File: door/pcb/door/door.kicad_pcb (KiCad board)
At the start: 2 copper layers, 57.8 x 45.7 mm, 43 parts, among them J2 Conn_01x06_Male, J3 DB9_Female_MountingHoles, J4 Conn_01x03_Male, J5 Screw_Terminal_01x02, J6 Screw_Terminal_01x02, J7 Power_in, U1 10uF, U2 STM32F303CBTx, U3 SN65HVD230, Y1 8 Mhz

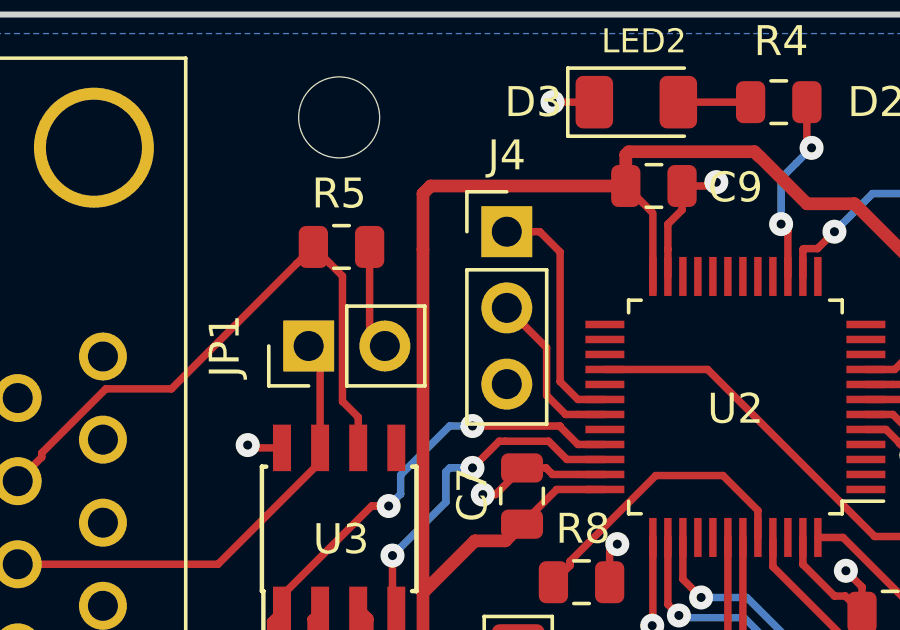
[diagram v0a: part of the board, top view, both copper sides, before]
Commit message: added silkscreen labels for the usart pin header
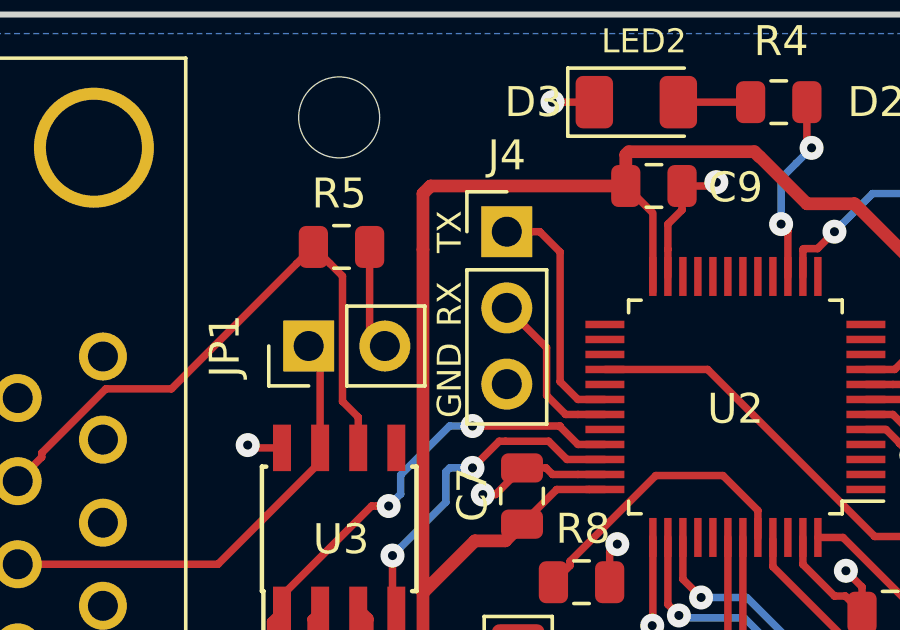
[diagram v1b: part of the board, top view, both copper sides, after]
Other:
- board text added: "RX"
- board text added: "TX"
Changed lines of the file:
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@@
   (general
     (thickness 1.6)
-    (drawings 25)
+    (drawings 28)
     (tracks 394)
     (zones 0)
@@
       (net 48 CAN_RX))
   )
+  (gr_text TX (at 113.919 78.994 90) (layer F.SilkS)
+    (effects (font (size 0.8 0.8) (thickness 0.1)))
+  )
+  (gr_text RX (at 113.919 81.407 90) (layer F.SilkS)
+    (effects (font (size 0.8 0.8) (thickness 0.1)))
+  )
+  (gr_text GND (at 113.919 83.947 90) (layer F.SilkS)
+    (effects (font (size 0.8 0.8) (thickness 0.1)))
+  )
   (gr_text "door V0.2" (at 124.46 93.472) (layer B.SilkS)

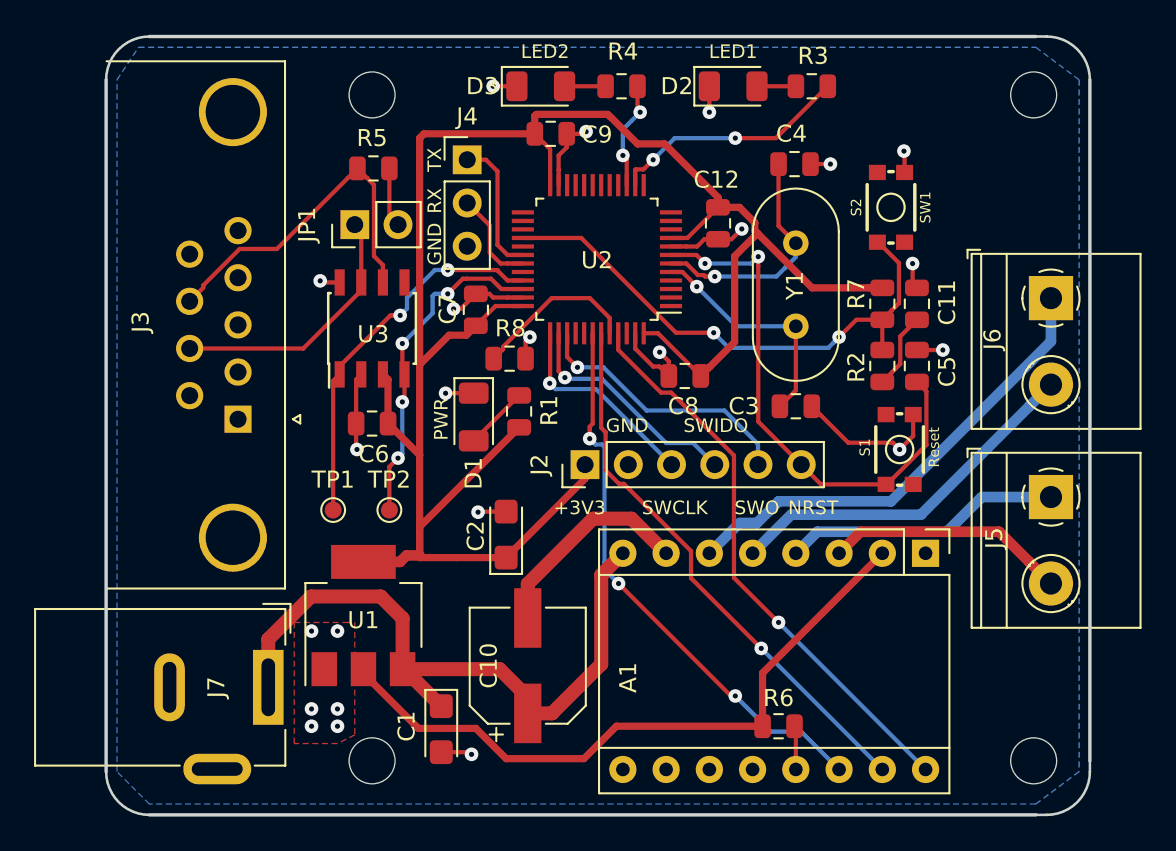
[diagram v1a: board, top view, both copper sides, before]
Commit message: changed pinout of DB-9 connector
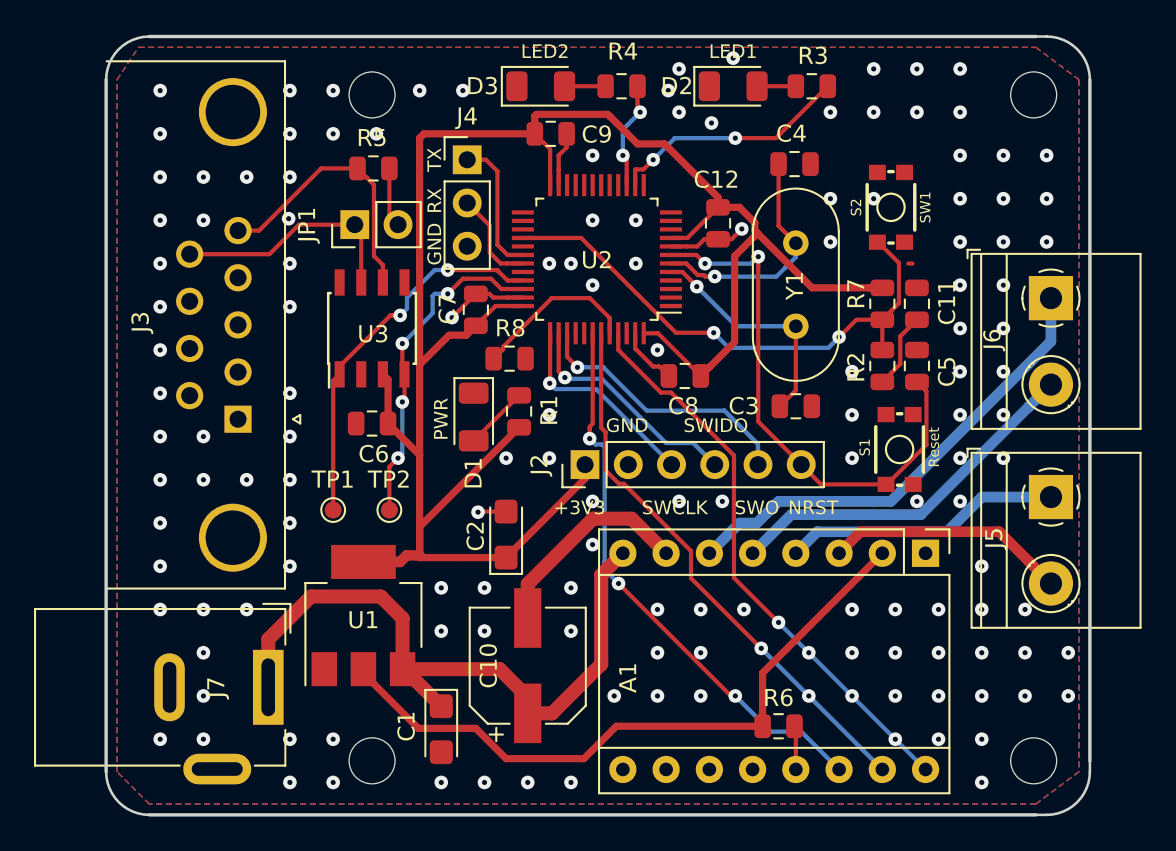
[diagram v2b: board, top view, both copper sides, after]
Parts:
- R1: value 250 -> 360
- U1: value 10uF -> LM1117DTX
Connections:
- J3 pad 1: Net-(J3-Pad1) -> GND
- J3 pad 5: GND -> /mcu/CANL
- J3 pad 7: /mcu/CANH -> Net-(J3-Pad7)
- J3 pad 8: /mcu/CANL -> Net-(J3-Pad8)
- J3 pad 9: Net-(J3-Pad9) -> /mcu/CANH
- J7 pad 1: +9V -> Net-(D4-Pad2)
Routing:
- net GND: track 60.8 -> 31.0 mm, vias 23 -> 140
- net /mcu/CANL: track 20.5 -> 15.8 mm
- net /mcu/CANH: track 15.5 -> 14.4 mm
- net DIR: vias 1 -> 4
- net STEP: vias 1 -> 2
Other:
- board text added: "door V0.3"
- board text removed: "door V0.2"

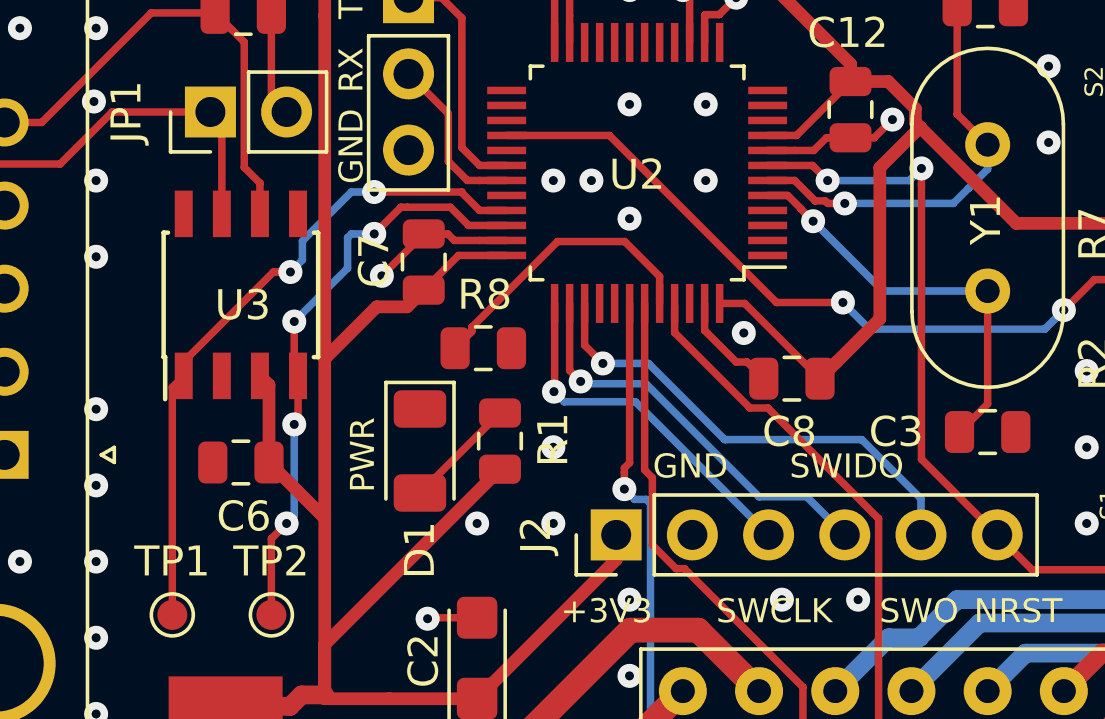
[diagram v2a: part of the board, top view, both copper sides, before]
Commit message: corrected error in Layout swido was connected with Can Rx
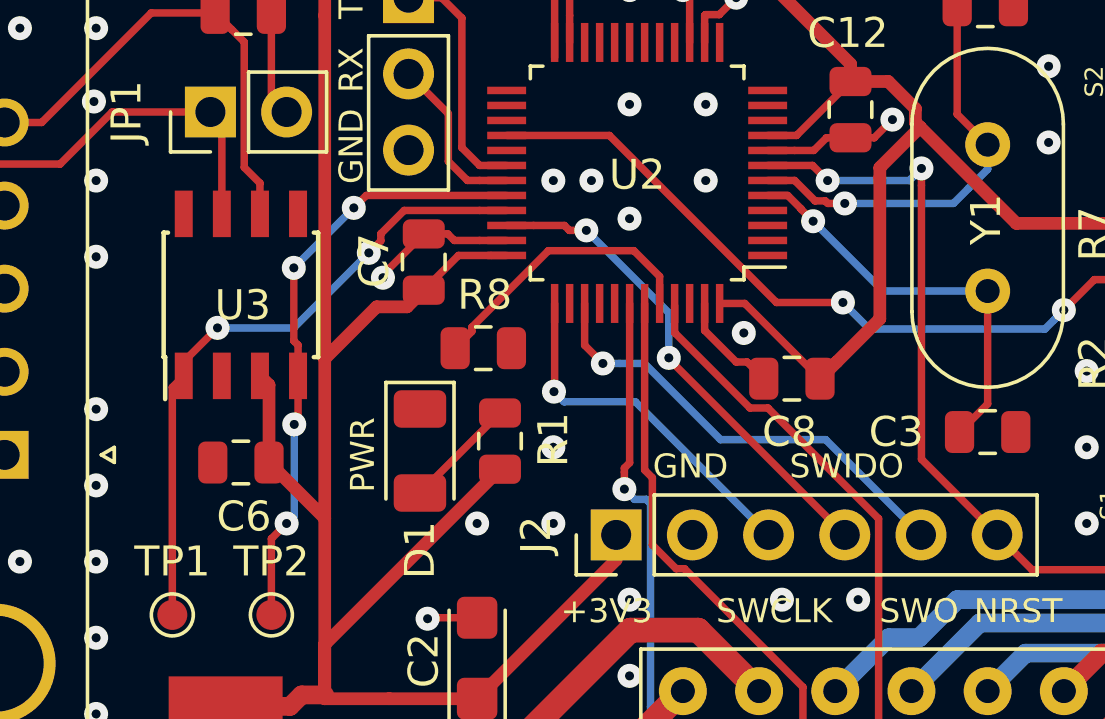
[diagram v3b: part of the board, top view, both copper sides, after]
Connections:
- U2 pad 32: Net-(U2-Pad32) -> CAN_RX
- U2 pad 34: CAN_RX -> SWIDO
- U2 pad 38: SWIDO -> Net-(U2-Pad38)
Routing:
- net SWIDO: track 13.7 -> 16.4 mm, vias 1 -> 2
- net CAN_TX: track 22.3 -> 21.6 mm
- net SWO: track 15.9 -> 15.2 mm
- net CAN_RX: track 19.9 -> 20.4 mm

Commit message: added polarity protection diode
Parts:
- added D4: STPS2L30, Diode_SMD:D_SMA, F.Cu at (109.5, 109.2)
- moved TP2 3.23 mm to (110.2, 96.5)
- moved TP1 3.10 mm to (107.5, 96.5)
- moved U1 2.72 mm to (110.8, 103.2), turned to 0 degrees
- moved J7 0.11 mm to (104.2, 110.0)
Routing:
- net +9V: track 41.5 -> 27.8 mm
- net Net-(D4-Pad2): track 0.00 -> 3.55 mm
- net CAN_TX: track 21.6 -> 18.7 mm
- net +3V3: track 158.1 -> 155.9 mm
- net GND: track 31.0 -> 29.4 mm, vias 140 -> 154
- net CAN_RX: track 20.4 -> 19.0 mm
- net DIR: vias 4 -> 1
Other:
- net class +3V3: trace_width 0.25 -> 0.425
- net class +9V: trace_width 0.625 -> 0.825
